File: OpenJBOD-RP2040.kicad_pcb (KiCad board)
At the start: 4 copper layers, 72.6 x 170 mm, 122 parts, among them J1 ATX-24, J2 Bus_PCI_Express_x1, J3 Conn_02x02_Counter_Clockwise, J4 UART, J5 USB_C_Receptacle_USB2.0_16P, J6 HR911105A, J9 TEMP1, Q1 MMBT3904, Q2 MMBT3904, SW1 TC-6615-6-260G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

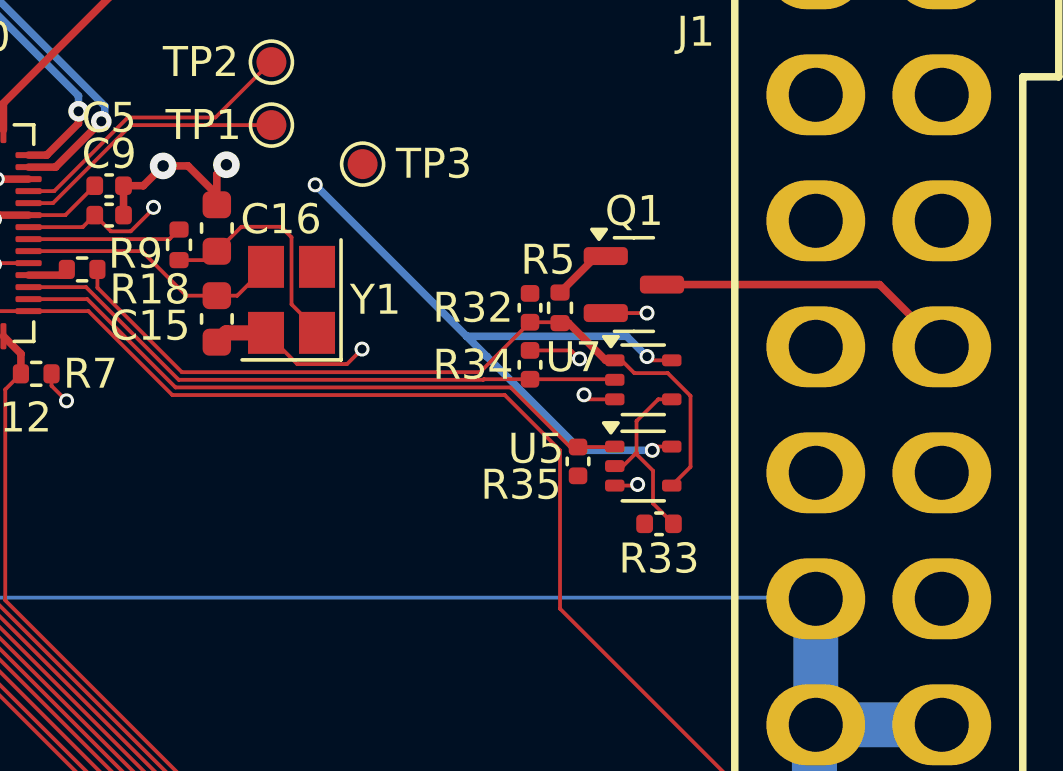
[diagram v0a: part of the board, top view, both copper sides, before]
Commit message: sch/pcb: SR latch caps
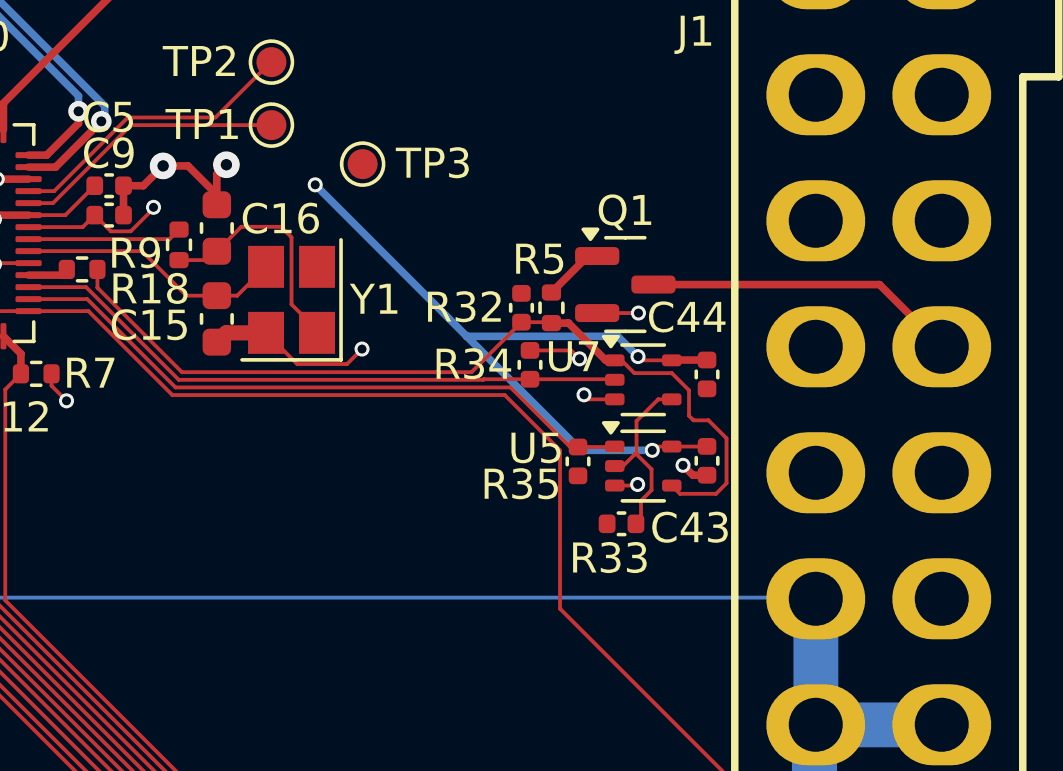
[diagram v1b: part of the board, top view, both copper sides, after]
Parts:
- added C43: 100nF, Capacitor_SMD:C_0402_1005Metric, F.Cu at (144.9, 126.7)
- added C44: 100nF, Capacitor_SMD:C_0402_1005Metric, F.Cu at (144.9, 123.8)
- moved R33 1.25 mm to (142.1, 128.8)
- moved Q1 0.29 mm to (142.2, 120.8)
- moved R32 0.29 mm to (138.7, 121.6)
- moved R5 0.29 mm to (139.7, 121.6)
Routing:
- net /LOUT: track 26.3 -> 28.9 mm
- net /+3.3vSB: track 233.6 -> 235.9 mm
- net GND: track 110.5 -> 111.4 mm, vias 59 -> 60
